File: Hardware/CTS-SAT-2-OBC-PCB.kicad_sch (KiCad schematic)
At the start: 0 parts

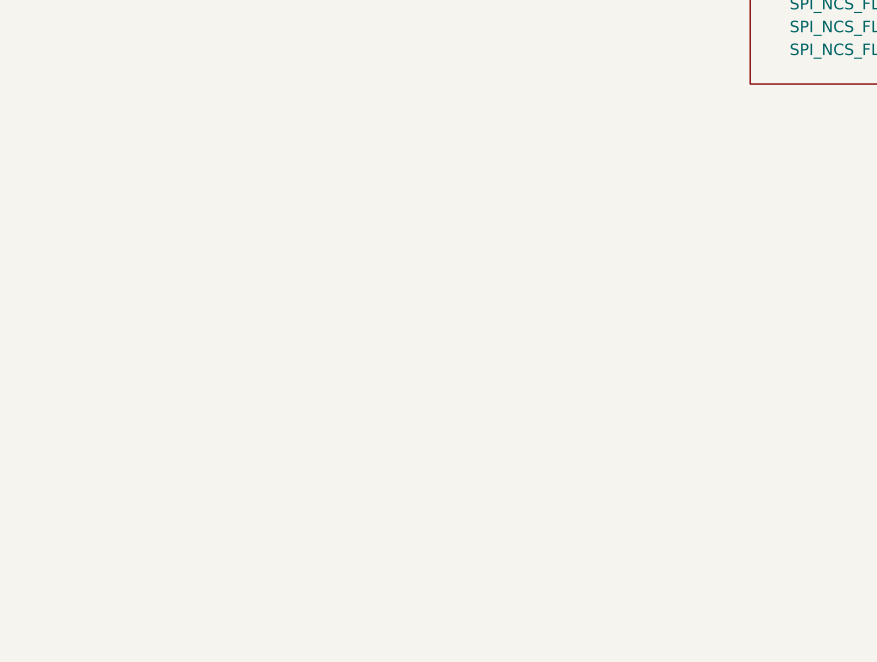
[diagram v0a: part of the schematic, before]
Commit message: Begin importing to SAT-2 PCB
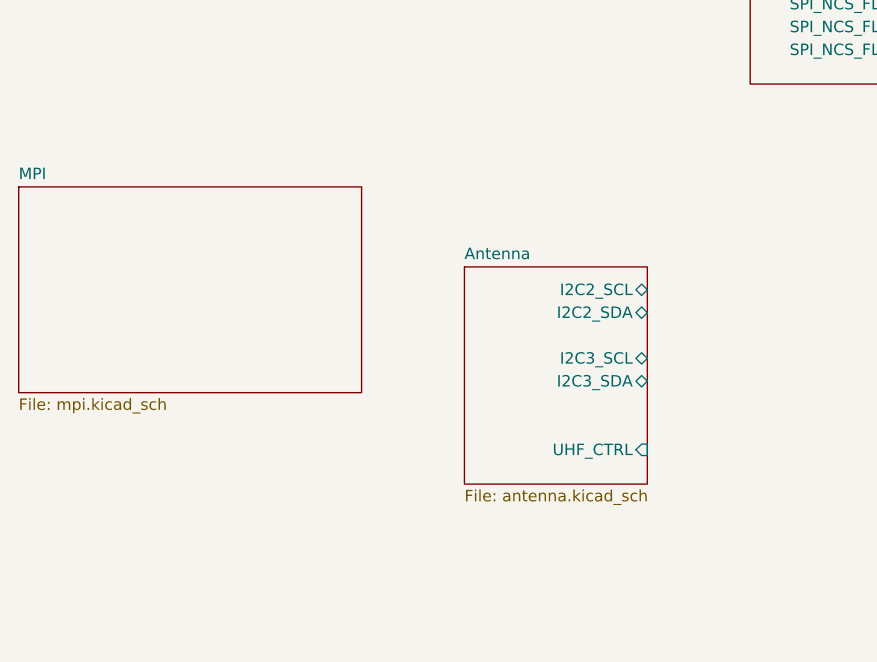
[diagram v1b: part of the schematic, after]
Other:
- added sheet Antenna (antenna.kicad_sch)
- added sheet MPI (mpi.kicad_sch)
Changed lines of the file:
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@@
+	)
+	(sheet
+		(at 29.21 118.11)
+		(size 38.1 22.86)
+		(exclude_from_sim no)
+		(in_bom yes)
+		(on_board yes)
+		(dnp no)
+		(fields_autoplaced yes)
+		(stroke
+			(width 0.1524)
+			(type solid)
+		)
+		(fill
+			(color 0 0 0 0.0000)
+		)
+		(property "Sheetname" "MPI"
+			(at 29.21 117.3984 0)
+			(effects
+				(font
+					(size 1.27 1.27)
+				)
+				(justify left bottom)
+			)
+		)
+		(property "Sheetfile" "mpi.kicad_sch"
+			(at 29.21 141.5546 0)
+			(effects
+				(font
+					(size 1.27 1.27)
+				)
+				(justify left top)
+			)
+		)
+		(instances
+			(project "CTS-SAT-2-OBC-PCB"
+				(path "/58243925-df8d-4fc1-899e-fce866d1d25a"
+					(page "7")
+				)
+			)
+		)
+	)
+	(sheet
+		(at 78.74 127)
+		(size 20.32 24.13)
+		(exclude_from_sim no)
+		(in_bom yes)
+		(on_board yes)
+		(dnp no)
+		(fields_autoplaced yes)
+		(stroke
+			(width 0.1524)
+			(type solid)
+		)
+		(fill
+			(color 0 0 0 0.0000)
+		)
+		(property "Sheetname" "Antenna"
+			(at 78.74 126.2884 0)
+			(effects
+				(font
+					(size 1.27 1.27)
+				)
+				(justify left bottom)
+			)
+		)
+		(property "Sheetfile" "antenna.kicad_sch"
+			(at 78.74 151.7146 0)
+			(effects
+				(font
+					(size 1.27 1.27)
+				)
+				(justify left top)
+			)
+		)
+		(pin "I2C2_SCL" bidirectional
+			(at 99.06 129.54 0)
+			(effects
+				(font
+					(size 1.27 1.27)
+				)
+				(justify right)
+			)
+		)
+		(pin "I2C2_SDA" bidirectional
+			(at 99.06 132.08 0)
+			(effects
+				(font
+					(size 1.27 1.27)
+				)
+				(justify right)
+			)
+		)
+		(pin "I2C3_SCL" bidirectional
+			(at 99.06 137.16 0)
+			(effects
+				(font
+					(size 1.27 1.27)
+				)
+				(justify right)
+			)
+		)
+		(pin "I2C3_SDA" bidirectional
+			(at 99.06 139.7 0)
+			(effects
+				(font
+					(size 1.27 1.27)
+				)
+				(justify right)
+			)
+		)
+		(pin "UHF_CTRL" input
+			(at 99.06 147.32 0)
+			(effects
+				(font
+					(size 1.27 1.27)
+				)
+				(justify right)
+			)
+		)
+		(instances
+			(project "CTS-SAT-2-OBC-PCB"
+				(path "/58243925-df8d-4fc1-899e-fce866d1d25a"
+					(page "6")
+				)
+			)
+		)
 	)
 	(sheet

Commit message: Connect connectors
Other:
- sheet Connectors ports: added BOOM_CTRL_1, BOOM_CTRL_2, CAM_EN, DEBUG_LED, GPS_PPS, MISO_LPUART1_RX, MISO_UART4_RX, MISO_UART5_RX, MISO_USART3_RX, MOSI_LPUART1_TX, MOSI_UART4_TX, MOSI_UART5_TX, MOSI_USART3_TX, NRST, RBF_1, SWCLK, SWDIO, SWO; removed 3V3_CAM
- sheet MPI ports: added MISO_MPI_RX_NEN, MISO_USART1_RX, MOSI_MPI_TX_EN, MOSI_USART1_TX; removed none
- sheet STM32 ports: added DEBUG_LED, SPI_NCS_FRAM_0, SPI_NCS_FRAM_1; removed none

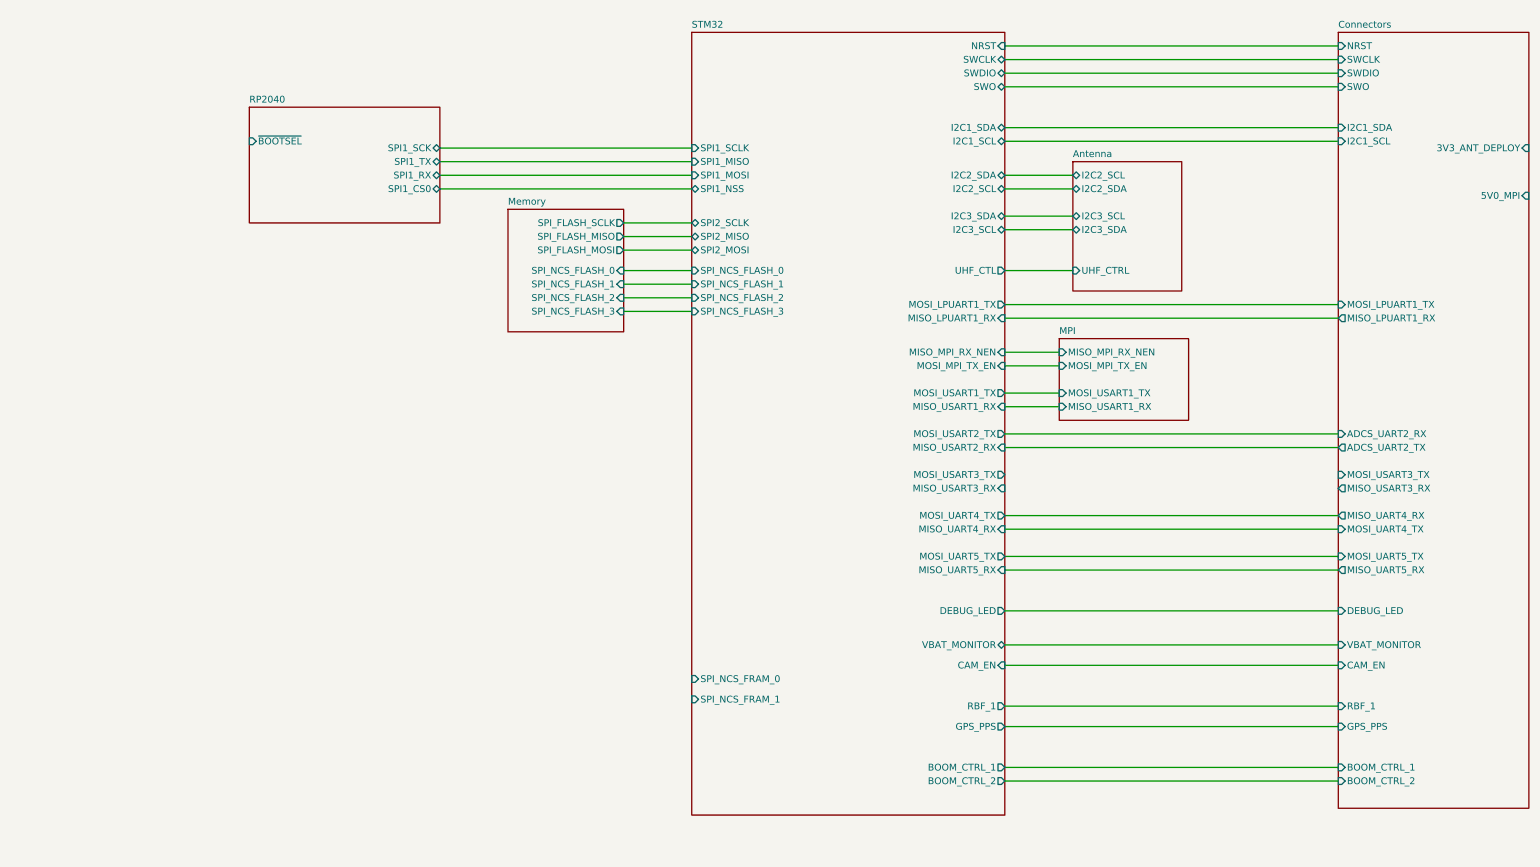
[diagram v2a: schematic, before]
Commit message: Add STM32 Reset Switch & RP2040 I2C pins
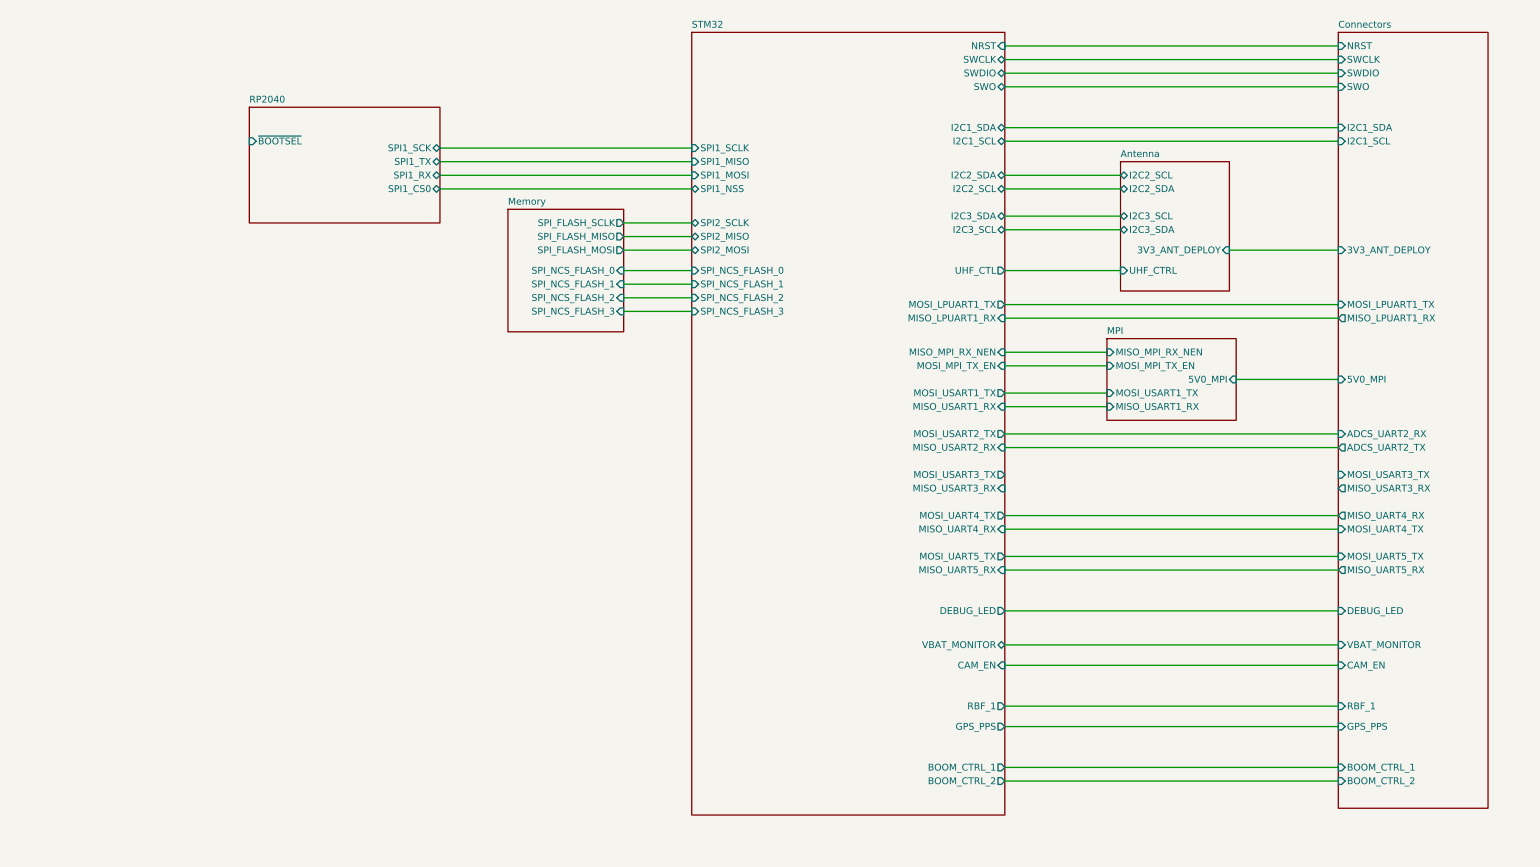
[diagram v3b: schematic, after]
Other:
- sheet Antenna ports: added 3V3_ANT_DEPLOY; removed none
- sheet MPI ports: added 5V0_MPI; removed none
- sheet STM32 ports: added none; removed SPI_NCS_FRAM_0, SPI_NCS_FRAM_1
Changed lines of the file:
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@@
 	(wire
 		(pts
-			(xy 203.2 120.65) (xy 213.36 120.65)
+			(xy 203.2 120.65) (xy 222.25 120.65)
 		)
 		(stroke
@@
 	(wire
 		(pts
-			(xy 203.2 80.01) (xy 215.9 80.01)
-		)
-		(stroke
-			(width 0)
-			(type default)
-		)
-	)
-	(wire
-		(pts
-			(xy 203.2 113.03) (xy 213.36 113.03)
+			(xy 203.2 80.01) (xy 224.79 80.01)
+		)
+		(stroke
+			(width 0)
+			(type default)
+		)
+	)
+	(wire
+		(pts
+			(xy 203.2 113.03) (xy 222.25 113.03)
 		)
 		(stroke
@@
 	(wire
 		(pts
+			(xy 245.11 91.44) (xy 265.43 91.44)
+		)
+		(stroke
+			(width 0)
+			(type default)
+		)
+	)
+	(wire
+		(pts
 			(xy 203.2 190.5) (xy 265.43 190.5)
 		)
@@
 	(wire
 		(pts
-			(xy 203.2 118.11) (xy 213.36 118.11)
+			(xy 203.2 118.11) (xy 222.25 118.11)
 		)
 		(stroke
@@
 	(wire
 		(pts
-			(xy 203.2 110.49) (xy 213.36 110.49)
-		)
-		(stroke
-			(width 0)
-			(type default)
-		)
-	)
-	(wire
-		(pts
-			(xy 203.2 95.25) (xy 215.9 95.25)
+			(xy 203.2 110.49) (xy 222.25 110.49)
+		)
+		(stroke
+			(width 0)
+			(type default)
+		)
+	)
+	(wire
+		(pts
+			(xy 203.2 95.25) (xy 224.79 95.25)
 		)
 		(stroke
@@
 	(wire
 		(pts
-			(xy 203.2 87.63) (xy 215.9 87.63)
+			(xy 203.2 87.63) (xy 224.79 87.63)
 		)
 		(stroke
@@
 	(wire
 		(pts
-			(xy 203.2 77.47) (xy 215.9 77.47)
+			(xy 203.2 77.47) (xy 224.79 77.47)
 		)
 		(stroke
@@
 	(wire
 		(pts
+			(xy 246.38 115.57) (xy 265.43 115.57)
+		)
+		(stroke
+			(width 0)
+			(type default)
+		)
+	)
+	(wire
+		(pts
 			(xy 132.08 91.44) (xy 144.78 91.44)
 		)
@@
 	(wire
 		(pts
-			(xy 203.2 85.09) (xy 215.9 85.09)
+			(xy 203.2 85.09) (xy 224.79 85.09)
 		)
 		(stroke
@@
 	)
 	(sheet
-		(at 213.36 107.95)
+		(at 222.25 107.95)
 		(size 24.13 15.24)
 		(exclude_from_sim no)
@@
 		)
 		(property "Sheetname" "MPI"
-			(at 213.36 107.2384 0)
+			(at 222.25 107.2384 0)
 			(effects
 				(font
@@
 		)
 		(property "Sheetfile" "mpi.kicad_sch"
-			(at 213.36 123.7746 0)
+			(at 222.25 123.7746 0)
 			(effects
 				(font
@@
 		)
 		(pin "MISO_MPI_RX_NEN" input
-			(at 213.36 110.49 180)
+			(at 222.25 110.49 180)
 			(effects
 				(font
@@
 		)
 		(pin "MISO_USART1_RX" input
-			(at 213.36 120.65 180)
+			(at 222.25 120.65 180)
 			(effects
 				(font
@@
 		)
 		(pin "MOSI_MPI_TX_EN" input
-			(at 213.36 113.03 180)
+			(at 222.25 113.03 180)
 			(effects
 				(font
@@
 		)
 		(pin "MOSI_USART1_TX" input
-			(at 213.36 118.11 180)
-			(effects
-				(font
-					(size 1.27 1.27)
-				)
-				(justify left)
+			(at 222.25 118.11 180)
+			(effects
+				(font
+					(size 1.27 1.27)
+				)
+				(justify left)
+			)
+		)
+		(pin "5V0_MPI" input
+			(at 246.38 115.57 0)
+			(effects
+				(font
+					(size 1.27 1.27)
+				)
+				(justify right)
 			)
 		)
@@
 	)
 	(sheet
-		(at 215.9 74.93)
+		(at 224.79 74.93)
 		(size 20.32 24.13)
 		(exclude_from_sim no)
@@
 		)
 		(property "Sheetname" "Antenna"
-			(at 215.9 74.2184 0)
+			(at 224.79 74.2184 0)
 			(effects
 				(font
@@
 		)
 		(property "Sheetfile" "antenna.kicad_sch"
-			(at 215.9 99.6446 0)
+			(at 224.79 99.6446 0)
 			(effects
 				(font
@@
 		)
 		(pin "I2C2_SCL" bidirectional
-			(at 215.9 77.47 180)
+			(at 224.79 77.47 180)
 			(effects
 				(font
@@
 		)
 		(pin "I2C2_SDA" bidirectional
-			(at 215.9 80.01 180)
+			(at 224.79 80.01 180)
 			(effects
 				(font
@@
 		)
 		(pin "I2C3_SCL" bidirectional
-			(at 215.9 85.09 180)
+			(at 224.79 85.09 180)
 			(effects
 				(font
@@
 		)
 		(pin "I2C3_SDA" bidirectional
-			(at 215.9 87.63 180)
+			(at 224.79 87.63 180)
 			(effects
 				(font
@@
 		)
 		(pin "UHF_CTRL" input
-			(at 215.9 95.25 180)
-			(effects
-				(font
-					(size 1.27 1.27)
-				)
-				(justify left)
+			(at 224.79 95.25 180)
+			(effects
+				(font
+					(size 1.27 1.27)
+				)
+				(justify left)
+			)
+		)
+		(pin "3V3_ANT_DEPLOY" input
+			(at 245.11 91.44 0)
+			(effects
+				(font
+					(size 1.27 1.27)
+				)
+				(justify right)
 			)
 		)
@@
 	(sheet
 		(at 265.43 50.8)
-		(size 35.56 144.78)
+		(size 27.94 144.78)
 		(exclude_from_sim no)
 		(in_bom yes)
@@
 		)
 		(pin "5V0_MPI" input
-			(at 300.99 81.28 0)
-			(effects
-				(font
-					(size 1.27 1.27)
-				)
-				(justify right)
+			(at 265.43 115.57 180)
+			(effects
+				(font
+					(size 1.27 1.27)
+				)
+				(justify left)
 			)
 		)
@@
 		)
 		(pin "3V3_ANT_DEPLOY" input
-			(at 300.99 72.39 0)
-			(effects
-				(font
-					(size 1.27 1.27)
-				)
-				(justify right)
+			(at 265.43 91.44 180)
+			(effects
+				(font
+					(size 1.27 1.27)
+				)
+				(justify left)
 			)
 		)
@@
 			)
 		)
-		(pin "SPI_NCS_FRAM_0" input
-			(at 144.78 171.45 180)
-			(effects
-				(font
-					(size 1.27 1.27)
-				)
-				(justify left)
-			)
-		)
-		(pin "SPI_NCS_FRAM_1" input
-			(at 144.78 175.26 180)
-			(effects
-				(font
-					(size 1.27 1.27)
-				)
-				(justify left)
-			)
-		)

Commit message: Move ANT to RP2040
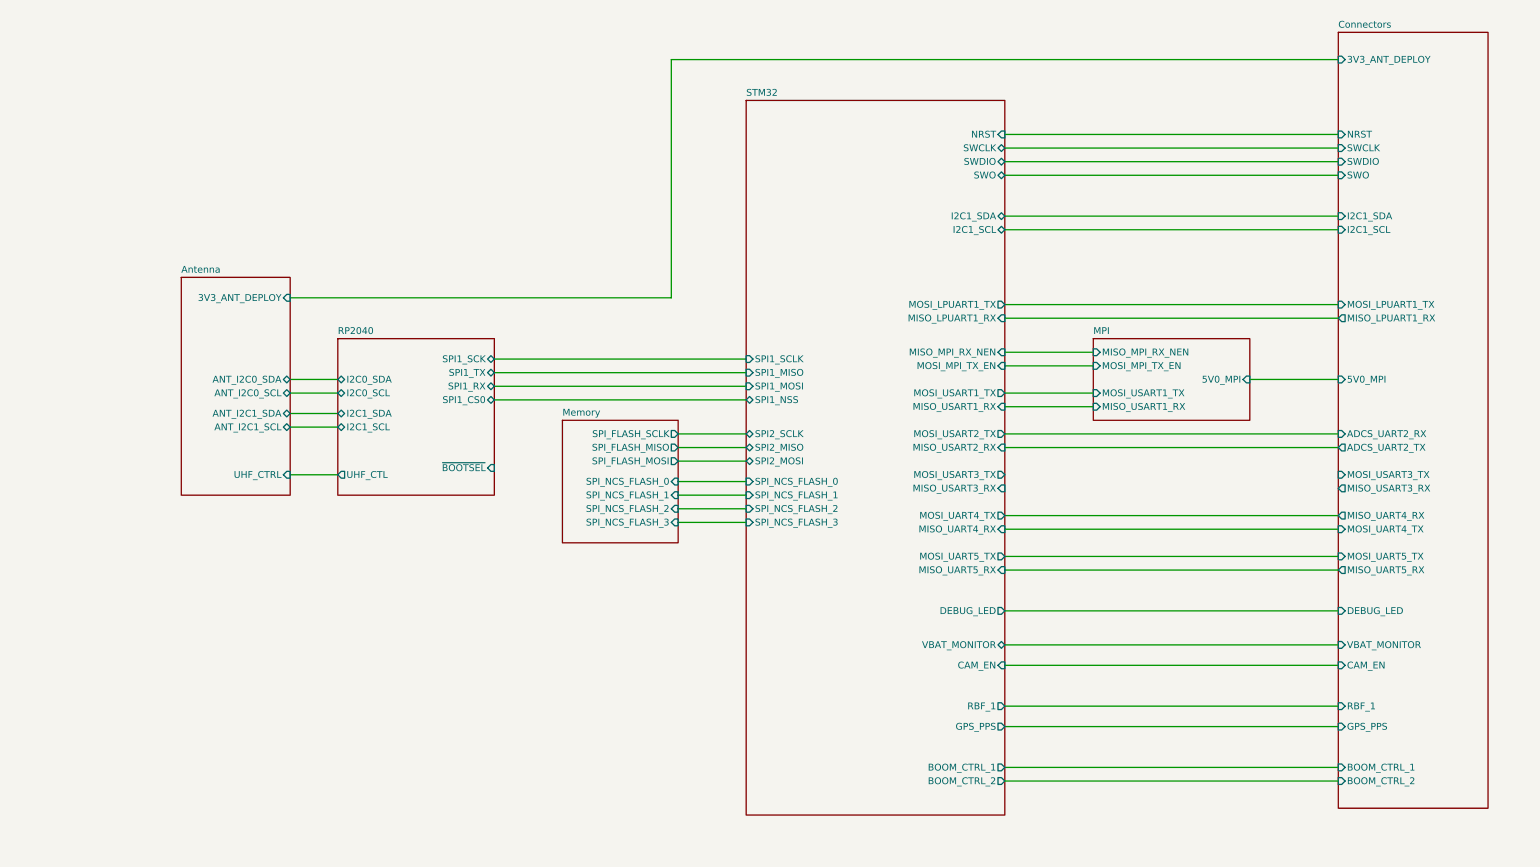
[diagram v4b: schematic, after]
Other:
- sheet Antenna ports: added ANT_I2C0_SCL, ANT_I2C0_SDA, ANT_I2C1_SCL, ANT_I2C1_SDA; removed I2C2_SCL, I2C2_SDA, I2C3_SCL, I2C3_SDA
- sheet RP2040 ports: added I2C0_SCL, I2C0_SDA, I2C1_SCL, I2C1_SDA, UHF_CTL; removed none
- sheet STM32 ports: added none; removed I2C2_SCL, I2C2_SDA, I2C3_SCL, I2C3_SDA, UHF_CTL

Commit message: Add RP2040 SWD
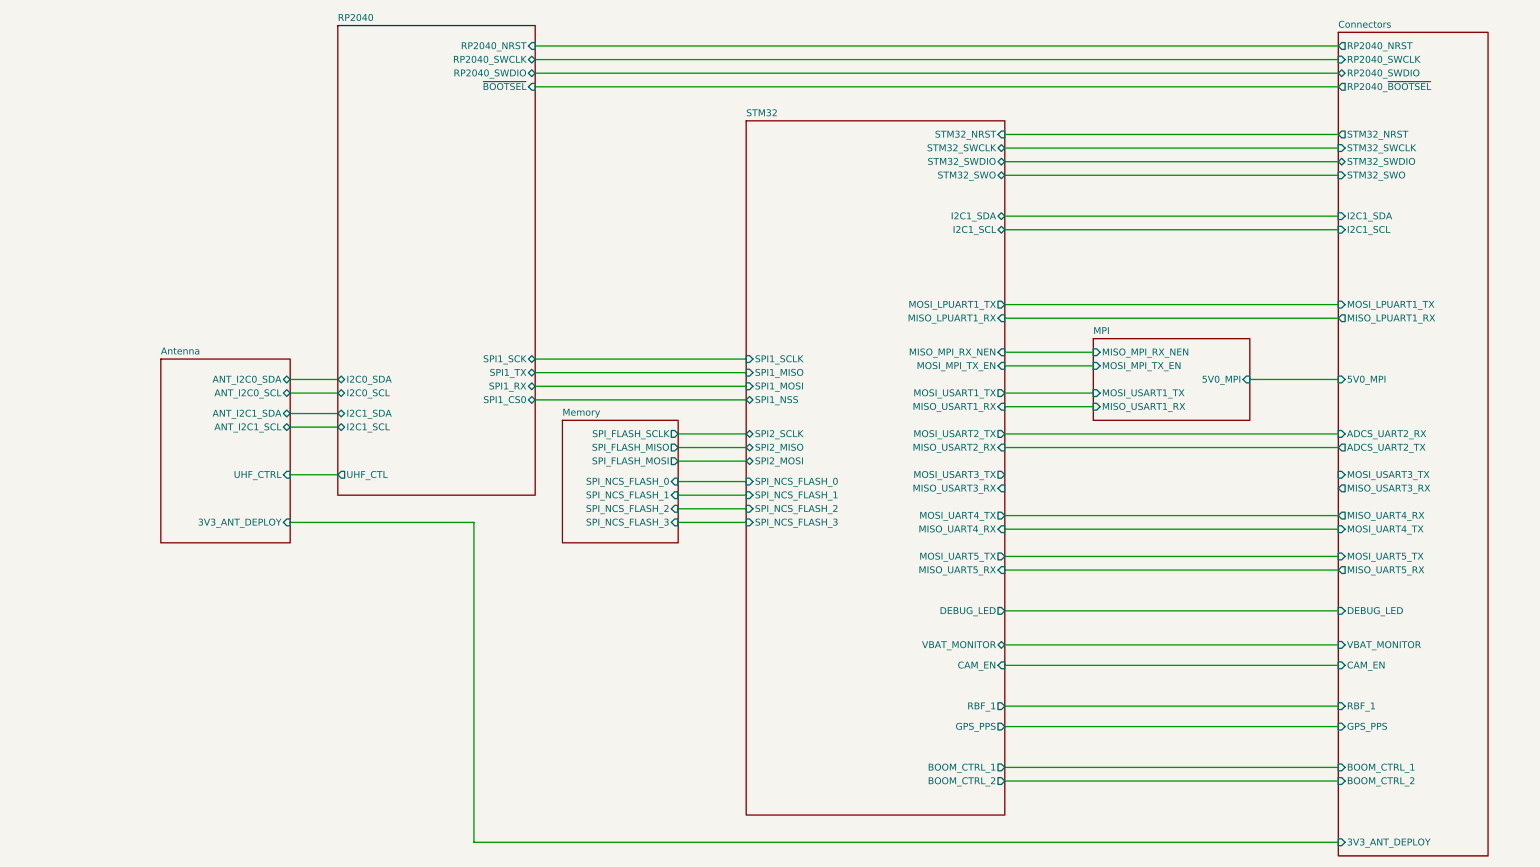
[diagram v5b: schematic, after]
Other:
- sheet Connectors ports: added RP2040_NRST, RP2040_SWCLK, RP2040_SWDIO, RP2040_~{BOOTSEL}, STM32_NRST, STM32_SWCLK, STM32_SWDIO, STM32_SWO; removed NRST, SWCLK, SWDIO, SWO
- sheet RP2040 ports: added RP2040_NRST, RP2040_SWCLK, RP2040_SWDIO; removed none
- sheet STM32 ports: added STM32_NRST, STM32_SWCLK, STM32_SWDIO, STM32_SWO; removed NRST, SWCLK, SWDIO, SWO
